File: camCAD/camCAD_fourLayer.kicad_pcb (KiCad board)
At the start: 4 copper layers, 89 x 54.6 mm, 70 parts, among them J1 USB C Charging Port, J2 JTAG header, J3 BATTERY, J4 ILI9341_Display_Header, SW1 NRST_SW, SW2 Pictures/Back, SW3 Forward, SW4 Backward, SW5 Flash/Delete, SW6 Shutter, U1 BQ24072RGTR Charging IC, U2 SC189ZSKTRT, U3 STM32F407ZGTx, U4 AP3602AKTR-G1 Charge Pump, U5 Flash LED, U6 ADA 254

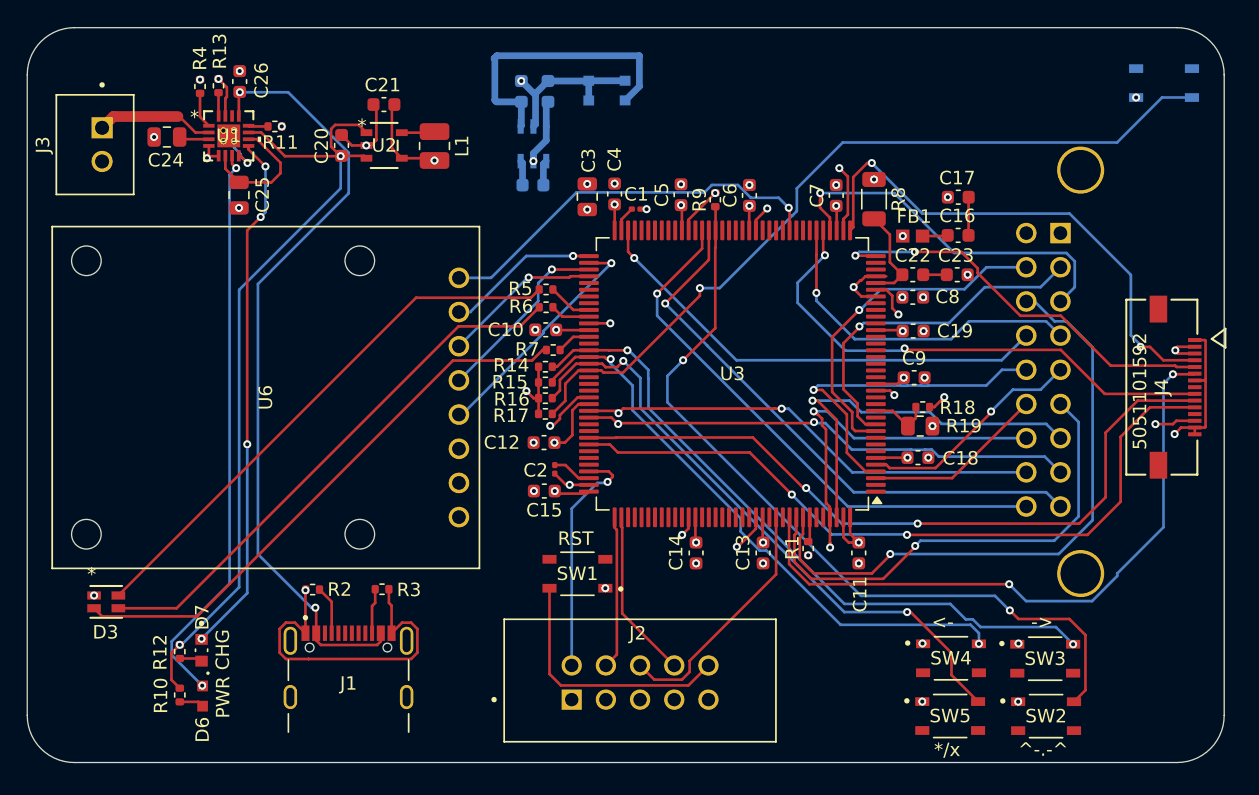
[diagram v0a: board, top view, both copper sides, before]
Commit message: Modified power trace widths and updated Readme
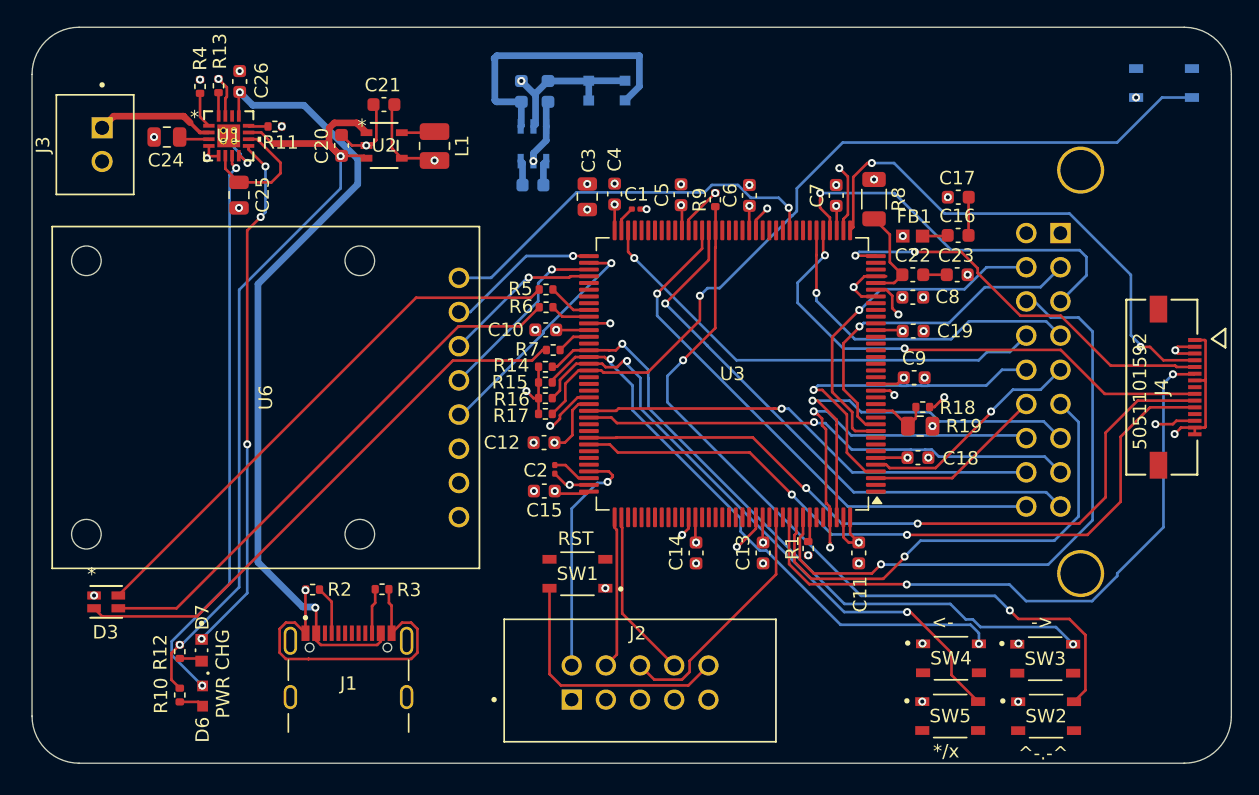
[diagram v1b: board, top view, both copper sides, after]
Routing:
- net PA4: track 27.5 -> 28.9 mm
- net BQ_IN: track 58.4 -> 59.4 mm
- net PG5: track 59.5 -> 60.2 mm
- net PB7: track 46.3 -> 47.0 mm
- net PC6: track 34.7 -> 34.5 mm, vias 2 -> 1
- net PC7: track 36.9 -> 36.8 mm, vias 2 -> 1
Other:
- board size 89 x 54.6 mm -> 89.1 x 54.7 mm
- board text added: "Siddharth Vasudevan"
- board text added: "熊猫"
